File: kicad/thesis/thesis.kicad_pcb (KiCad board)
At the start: 2 copper layers, 100 x 75 mm, 31 parts, among them J1 Conn_01x01_Socket, J10 Conn_01x01_Socket, J2 Conn_01x01_Socket, J3 Conn_01x07_Socket, J4 Conn_01x04_Socket, J5 Conn_01x01_Socket, J6 Conn_01x01_Socket, J7 Conn_01x01_Socket, J8 Conn_01x01_Socket, J9 Conn_01x03_Socket, Q1 IRLZB8721, U1 INA219AxD

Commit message: Added Labels for the GPIO and other Header socket
ge pa limpyo ra
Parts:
- moved J1 11.5 mm to (190.2, 124.0)
- moved J10 10.8 mm to (163.6, 114.3)
- moved J2 0.35 mm to (155.5, 131.6)
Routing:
- net Net-(J10-Pin_1): track 14.0 -> 5.32 mm
- net Vin: track 4.80 -> 7.16 mm
- net GND: track 292.6 -> 294.6 mm
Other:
- board text added: "A3"
- board text added: "A6"
- board text added: "A7"
- board text added: "D0"
- board text added: "D1"
- board text added: "HALL SENSOR"
- board text added: "Vin"
- board text added: "Vref"
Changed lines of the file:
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@@
 		(tags "Through hole socket strip THT 1x01 2.54mm single row")
 		(property "Reference" "J5"
-			(at 0 -2.77 0)
+			(at -2.7 -0.1 0)
 			(layer "F.SilkS")
 			(effects
@@
 	(footprint "Connector_PinSocket_2.54mm:PinSocket_1x01_P2.54mm_Vertical"
 		(layer "F.Cu")
-		(at 155.5 131.25)
+		(at 155.5 131.6)
 		(descr "Through hole straight socket strip, 1x01, 2.54mm pitch, single row (from Kicad 4.0.7), script generated")
 		(tags "Through hole socket strip THT 1x01 2.54mm single row")
 		(property "Reference" "J2"
-			(at 0 2.75 0)
+			(at 0 -2.55 0)
 			(layer "F.SilkS")
 			(effects
@@
 		)
 		(property "Value" "Conn_01x01_Socket"
-			(at 0 2.77 0)
+			(at 0.3 -4.25 0)
 			(layer "F.Fab")
 			(effects
@@
 		)
 		(fp_text user "${REFERENCE}"
-			(at 0 8.89 180)
+			(at 0 -4.22 180)
 			(layer "F.Fab")
 			(effects
@@
 	(footprint "Connector_PinSocket_2.54mm:PinSocket_1x01_P2.54mm_Vertical"
 		(layer "F.Cu")
-		(at 181.25 131.25)
+		(at 190.2 124)
 		(descr "Through hole straight socket strip, 1x01, 2.54mm pitch, single row (from Kicad 4.0.7), script generated")
 		(tags "Through hole socket strip THT 1x01 2.54mm single row")
 		(property "Reference" "J1"
-			(at 0 -2.41 0)
+			(at 2.75 0.15 0)
 			(layer "F.SilkS")
 			(effects
@@
 		)
 		(property "Value" "Conn_01x01_Socket"
-			(at 0 2.77 0)
+			(at -9.75 0.95 0)
 			(layer "F.Fab")
 			(effects
@@
 		(tags "THT Terminal Block Phoenix MKDS-1,5-2-5.08 pitch 5.08mm size 10.2x9.8mm drill 1.3mm pad 2.6mm")
 		(property "Reference" "TH1"
-			(at 2.54 -6.32 0)
+			(at 9.2 -0.2 0)
 			(layer "F.SilkS")
 			(effects
@@
 		(tags "Through hole socket strip THT 1x01 2.54mm single row")
 		(property "Reference" "J6"
-			(at 0 -2.77 0)
+			(at 2.75 -0.1 0)
 			(layer "F.SilkS")
 			(effects
@@
 		(tags "Through hole socket strip THT 1x07 2.54mm single row")
 		(property "Reference" "J3"
-			(at 0 -2.77 0)
+			(at 2.5 -0.15 0)
 			(layer "F.SilkS")
 			(effects
@@
 		(tags "THT Terminal Block Phoenix MKDS-1,5-2-5.08 pitch 5.08mm size 10.2x9.8mm drill 1.3mm pad 2.6mm")
 		(property "Reference" "TH2"
-			(at 2.54 -6.32 0)
+			(at -4.555 -0.2725 0)
 			(layer "F.SilkS")
 			(effects
@@
 	(footprint "Connector_PinSocket_2.54mm:PinSocket_1x01_P2.54mm_Vertical"
 		(layer "F.Cu")
-		(at 171.7 121.5)
+		(at 163.6 114.3)
 		(descr "Through hole straight socket strip, 1x01, 2.54mm pitch, single row (from Kicad 4.0.7), script generated")
 		(tags "Through hole socket strip THT 1x01 2.54mm single row")
@@
 		(layer "User.2")
 	)
+	(gr_text "D0"
+		(at 118.5 85.5 0)
+		(layer "User.1")
+		(effects
+			(font
+				(size 1 1)
+				(thickness 0.15)
+			)
+			(justify left bottom)
+		)
+	)
 	(gr_text "D10"
 		(at 119.5 117 0)
@@
 		)
 	)
+	(gr_text "D1"
+		(at 123.2 85.5 0)
+		(layer "User.1")
+		(effects
+			(font
+				(size 1 1)
+				(thickness 0.15)
+			)
+			(justify left bottom)
+		)
+	)
 	(gr_text "GND"
 		(at 150 132 0)
@@
 		)
 	)
+	(gr_text "A7"
+		(at 155.5 94.4 0)
+		(layer "User.1")
+		(effects
+			(font
+				(size 1 1)
+				(thickness 0.15)
+			)
+			(justify left bottom)
+		)
+	)
+	(gr_text "A6"
+		(at 155.5 97.2 0)
+		(layer "User.1")
+		(effects
+			(font
+				(size 1 1)
+				(thickness 0.15)
+			)
+			(justify left bottom)
+		)
+	)
+	(gr_text "A3"
+		(at 155.5 99.6 0)
+		(layer "User.1")
+		(effects
+			(font
+				(size 1 1)
+				(thickness 0.15)
+			)
+			(justify left bottom)
+		)
+	)
+	(gr_text "Vin"
+		(at 155.6 89.1 0)
+		(layer "User.1")
+		(effects
+			(font
+				(size 1 1)
+				(thickness 0.15)
+			)
+			(justify left bottom)
+		)
+	)
+	(gr_text "Vref"
+		(at 155.7 118.9 0)
+		(layer "User.1")
+		(effects
+			(font
+				(size 1 1)
+				(thickness 0.15)
+			)
+			(justify left bottom)
+		)
+	)
+	(gr_text "HALL SENSOR"
+		(at 165.5 115 0)
+		(layer "User.1")
+		(effects
+			(font
+				(size 1 1)
+				(thickness 0.15)
+			)
+			(justify left bottom)
+		)
+	)
 	(gr_text "PWR"
-		(at 176.25 132 0)
+		(at 185.2 124.4 0)
 		(layer "User.1")
 		(effects
@@
 	)
 	(segment
+		(start 125.8 130.3)
+		(end 115.1 119.6)
+		(width 0.5)
+		(layer "B.Cu")
+		(net "GND")
+	)
+	(segment
 		(start 121.3 82.9)
 		(end 126.1 82.9)
@@
 	)
 	(segment
-		(start 132.4 130.3)
-		(end 125.8 130.3)
-		(width 0.5)
-		(layer "B.Cu")
-		(net "GND")
-	)
-	(segment
 		(start 118.42 66)
 		(end 118.42 69.82)
@@
 	)
 	(segment
-		(start 115.1 119.6)
-		(end 115.1 110.71)
-		(width 0.5)
-		(layer "B.Cu")
-		(net "GND")
-	)
-	(segment
-		(start 163.67 131.25)
-		(end 166.92 128)
-		(width 0.5)
-		(layer "B.Cu")
-		(net "GND")
-	)
-	(segment
-		(start 166.21 131.25)
-		(end 163.67 131.25)
+		(start 132.4 130.3)
+		(end 125.8 130.3)
 		(width 0.5)
 		(layer "B.Cu")
@@
 	)
 	(segment
-		(start 133.35 131.25)
-		(end 132.4 130.3)
+		(start 115.1 119.6)
+		(end 115.1 110.71)
 		(width 0.5)
 		(layer "B.Cu")
@@
 	)
 	(segment
-		(start 179.62 128)
-		(end 176.37 131.25)
+		(start 160.7 89.6)
+		(end 160.7 104.4)
 		(width 0.5)
 		(layer "B.Cu")
@@
 	)
 	(segment
-		(start 160.7 89.6)
-		(end 160.7 104.4)
+		(start 120.31 93.77)
+		(end 107.5 80.96)
 		(width 0.5)
 		(layer "B.Cu")
@@
 	)
 	(segment
-		(start 120.31 93.77)
-		(end 107.5 80.96)
+		(start 179.62 128)
+		(end 176.02 131.6)
 		(width 0.5)
 		(layer "B.Cu")
@@
 	)
 	(segment
-		(start 155.5 131.25)
-		(end 163.67 131.25)
+		(start 155.5 131.6)
+		(end 163.67 131.6)
 		(width 0.5)
 		(layer "B.Cu")
@@
 	(segment
 		(start 155.5 131.25)
-		(end 133.35 131.25)
+		(end 154.95 131.8)
 		(width 0.5)
 		(layer "B.Cu")
@@
 	)
 	(segment
+		(start 154.95 131.8)
+		(end 133.9 131.8)
+		(width 0.5)
+		(layer "B.Cu")
+		(net "GND")
+	)
+	(segment
 		(start 169.46 128)
 		(end 166.21 131.25)
@@
 	)
 	(segment
-		(start 154.62 91.22)
-		(end 156 92.6)
+		(start 166.21 131.25)
+		(end 165.86 131.6)
 		(width 0.5)
 		(layer "B.Cu")
@@
 	)
 	(segment
-		(start 126.1 82.9)
-		(end 133.2 82.9)
+		(start 154.62 91.22)
+		(end 156 92.6)
 		(width 0.5)
 		(layer "B.Cu")
@@
 	)
 	(segment
-		(start 125.8 130.3)
-		(end 115.1 119.6)
+		(start 126.1 82.9)
+		(end 133.2 82.9)
 		(width 0.5)
 		(layer "B.Cu")
@@
 	)
 	(segment
-		(start 176.37 131.25)
-		(end 166.21 131.25)
+		(start 163.32 131.6)
+		(end 166.92 128)
 		(width 0.5)
 		(layer "B.Cu")
@@
 	)
 	(segment
-		(start 115.1 110.71)
-		(end 120.31 105.5)
+		(start 133.9 131.8)
+		(end 132.4 130.3)
 		(width 0.5)
 		(layer "B.Cu")
@@
 	)
 	(segment
+		(start 115.1 110.71)
+		(end 120.31 105.5)
+		(width 0.5)
+		(layer "B.Cu")
+		(net "GND")
+	)
+	(segment
 		(start 124.1 81.1)
 		(end 125.9 82.9)
@@
 	)
 	(segment
+		(start 165.86 131.6)
+		(end 163.32 131.6)
+		(width 0.5)
+		(layer "B.Cu")
+		(net "GND")
+	)
+	(segment
 		(start 134.965 66.3275)
 		(end 137.8925 63.4)
@@
 	)
 	(segment
+		(start 176.02 131.6)
+		(end 165.86 131.6)
+		(width 0.5)
+		(layer "B.Cu")
+		(net "GND")
+	)
+	(segment
 		(start 119.36 80.96)
 		(end 121.3 82.9)
@@
 	)
 	(segment
-		(start 181.25 131.25)
-		(end 181.45 131.25)
+		(start 188.7 124)
+		(end 190.2 124)
 		(width 0.5)
 		(layer "B.Cu")
@@
 	)
 	(segment
-		(start 181.45 131.25)
-		(end 184.7 128)
+		(start 184.7 128)
+		(end 188.7 124)
 		(width 0.5)
 		(layer "B.Cu")
@@
 	)
 	(segment
-		(start 171.7 121.5)
-		(end 171.7 115.79)
+		(start 165.81 112.09)
+		(end 163.6 114.3)
 		(width 0.25)
 		(layer "B.Cu")
@@
 	)
 	(segment
-		(start 171.7 115.79)
-		(end 165.81 109.9)
+		(start 165.81 109.9)
+		(end 165.81 112.09)
 		(width 0.25)
 		(layer "B.Cu")

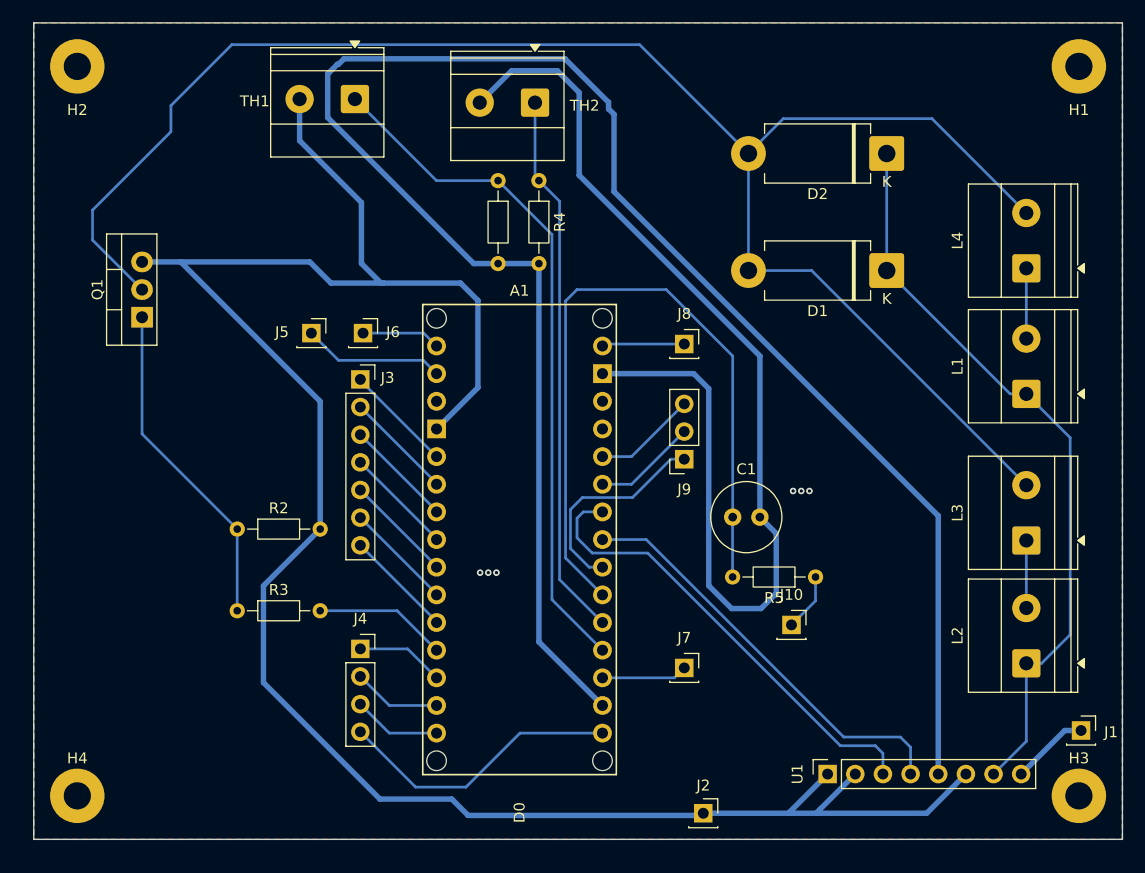
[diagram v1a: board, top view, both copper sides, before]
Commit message: Added 5 pins for 3.3 and GND
Also added folder for pcb printed under thesis gerber
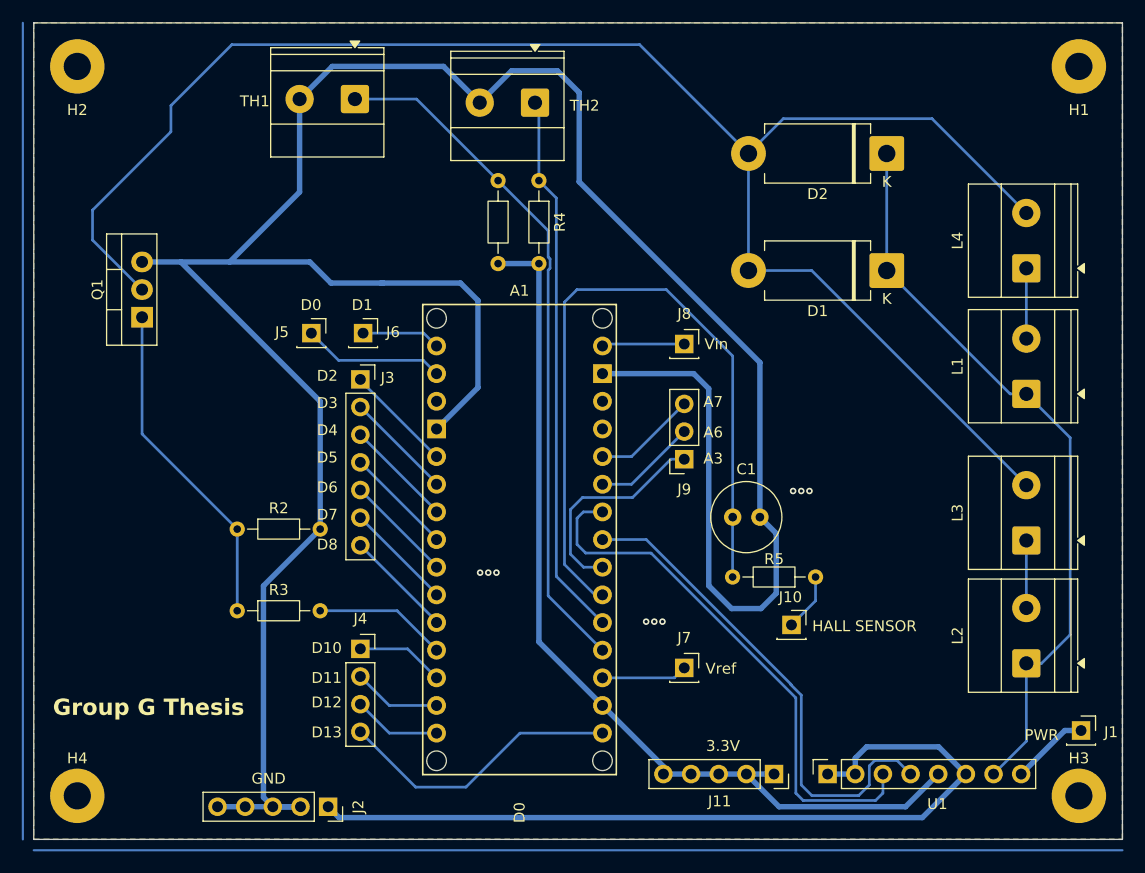
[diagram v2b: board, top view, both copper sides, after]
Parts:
- added J11: Conn_01x05_Socket, Connector_PinSocket_2.54mm:PinSocket_1x05_P2.54mm_Vertical, F.Cu at (162.0, 128.0)
- J2: value Conn_01x01_Socket -> Conn_01x05_Socket; footprint Connector_PinSocket_2.54mm:PinSocket_1x01_P2.54mm_Vertical -> Connector_PinSocket_2.54mm:PinSocket_1x05_P2.54mm_Vertical
- moved J2 34.5 mm to (121.0, 131.0), turned to -90 degrees
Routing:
- net +3.3V: track 174.2 -> 85.6 mm
- net GND: track 294.6 -> 327.7 mm, vias 6 -> 9
- net /A1: track 42.6 -> 50.0 mm
- net /A0: track 38.7 -> 45.8 mm
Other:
- board text added: "3.3V"

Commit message: Updated PCB
fixed INA and change electromagnet orientation and fixed pin placement
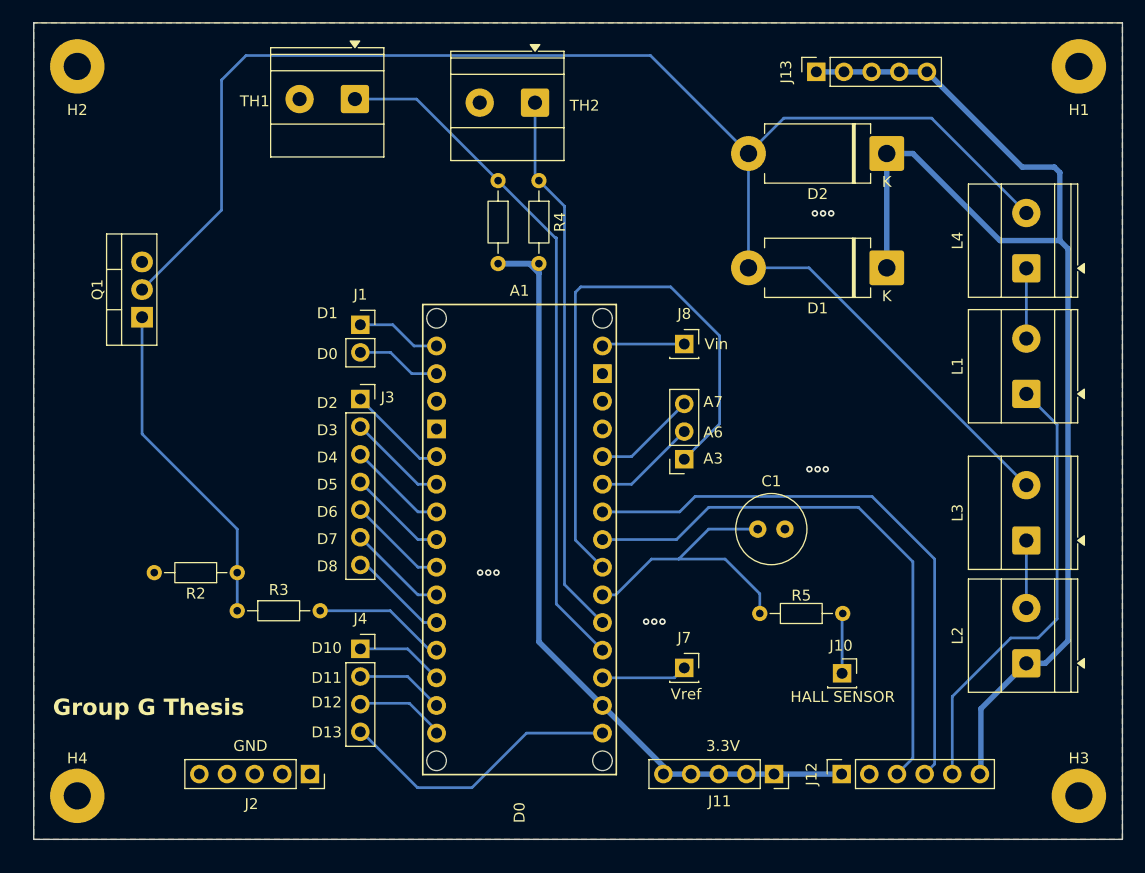
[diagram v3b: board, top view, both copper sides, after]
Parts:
- removed J5, J6: Conn_01x01_Socket, Connector_PinSocket_2.54mm:PinSocket_1x01_P2.54mm_Vertical
- removed U1: INA219AxD, Connector_PinSocket_2.54mm:PinSocket_1x08_P2.54mm_Vertical
- added J12: INA219, Connector_PinSocket_2.54mm:PinSocket_1x06_P2.54mm_Vertical, F.Cu at (168.2, 128.0)
- added J13: 12V, Connector_PinSocket_2.54mm:PinSocket_1x05_P2.54mm_Vertical, F.Cu at (165.9, 63.5)
- J1: value Conn_01x01_Socket -> Conn_01x02_Socket; footprint Connector_PinSocket_2.54mm:PinSocket_1x01_P2.54mm_Vertical -> Connector_PinSocket_2.54mm:PinSocket_1x02_P2.54mm_Vertical
- moved J1 76.0 mm to (124.0, 86.7)
- moved J10 6.44 mm to (168.2, 118.8)
- moved R5 4.18 mm to (168.3, 113.2)
- moved R2 4.00 mm to (112.7, 109.5), turned to 180 degrees
- moved J2 3.43 mm to (119.4, 128.0)
- moved C1 2.55 mm to (160.5, 105.5)
- moved J3 1.80 mm to (124.0, 93.5)
- moved D1 0.25 mm to (172.3, 81.5)
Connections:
- A1 pad A4: /A0 -> /A4
- A1 pad A5: /A1 -> /A5
- D1 pad 1: Net-(D1-K) -> Vin
- D2 pad 1: Net-(D1-K) -> Vin
- J1 pad 1: Vin -> Net-(A1-D1/TX)
- L1 pad 1: Net-(D1-K) -> Net-(J12-Pin_5)
- L2 pad 1: Net-(D1-K) -> Vin
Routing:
- net GND: track 327.7 -> 0.00 mm, vias 9 -> 12
- net Vin: track 7.16 -> 115.9 mm
- net Net-(D1-K): track 68.6 -> 0.00 mm
- net /A5: track 0.00 -> 53.6 mm
- net /A4: track 0.00 -> 51.9 mm
- net /A1: track 50.0 -> 0.00 mm
- net /A0: track 45.8 -> 0.00 mm
- net Net-(J12-Pin_5): track 0.00 -> 41.9 mm
- net Net-(A1-PadA2): track 67.5 -> 27.6 mm
- net Net-(J9-Pin_1): track 19.9 -> 54.3 mm
- net +3.3V: track 85.6 -> 75.9 mm
- net Net-(D1-A): track 156.2 -> 150.1 mm
- net Net-(A1-D0/RX): track 13.0 -> 7.81 mm
- net Net-(J3-Pin_7): track 9.99 -> 9.28 mm
- net Net-(J3-Pin_4): track 9.99 -> 9.28 mm
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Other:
- board text removed: "PWR"

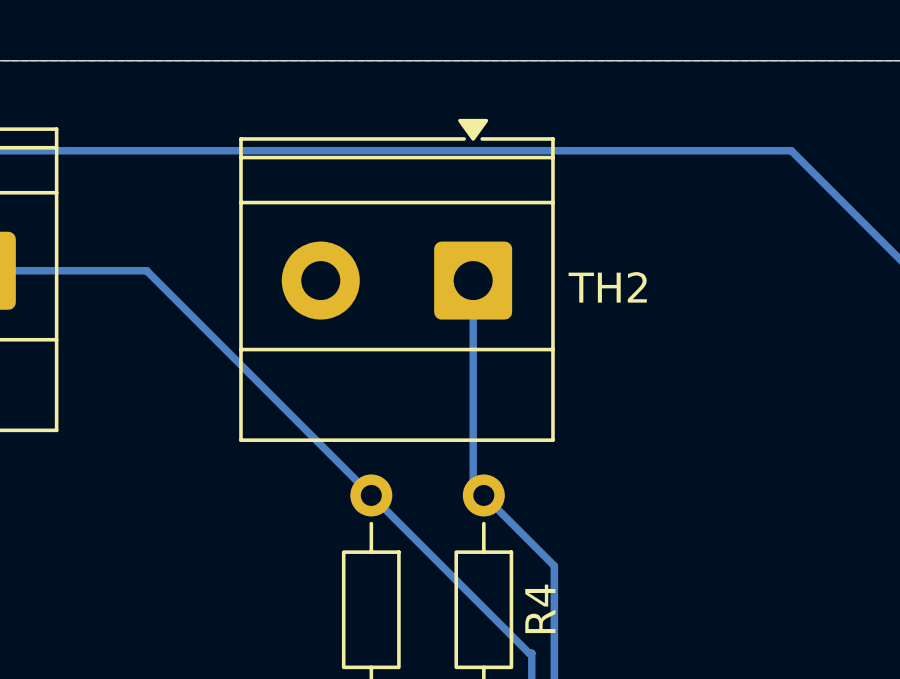
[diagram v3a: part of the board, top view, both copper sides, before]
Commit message: aligned terminal blocks
fixed misalignment
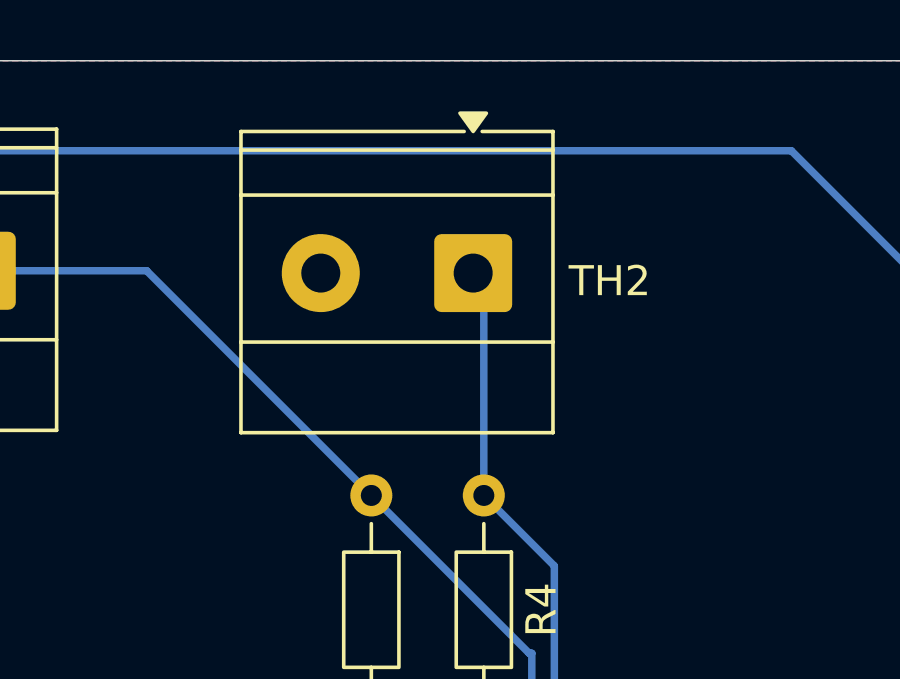
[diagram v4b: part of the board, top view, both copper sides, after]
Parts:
- moved TH2 0.25 mm to (140.0, 66.1)
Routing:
- net Net-(A1-PadA1): track 50.3 -> 51.1 mm
